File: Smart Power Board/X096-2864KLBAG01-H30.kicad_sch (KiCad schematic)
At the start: 12 parts, among them Q1 FDN338P, Q4 FDN335N

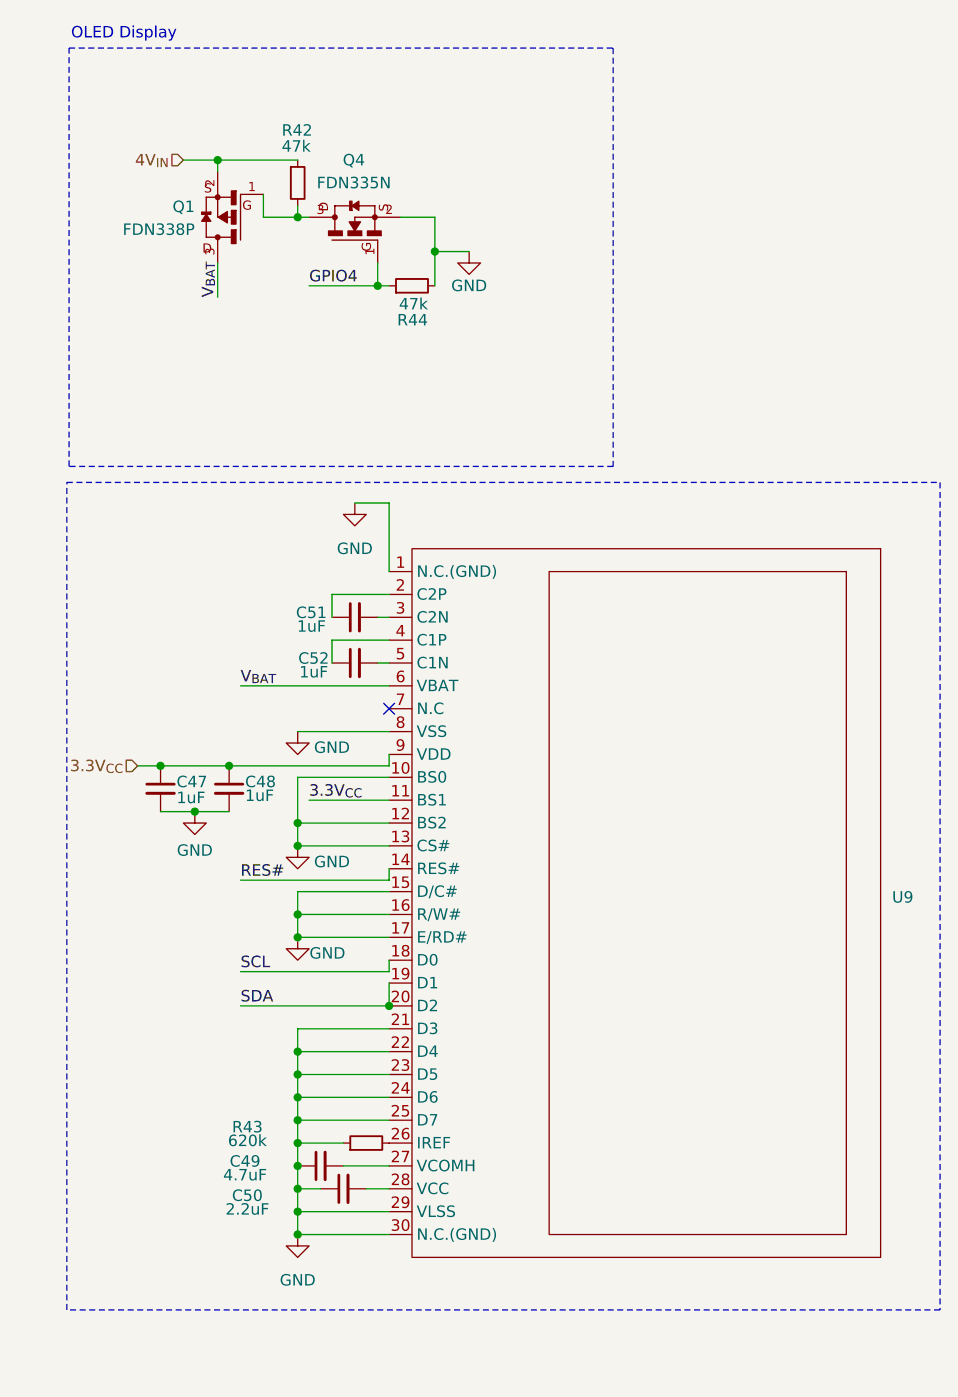
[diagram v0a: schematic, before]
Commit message: Feat[SmartPowerBoard]: Routing
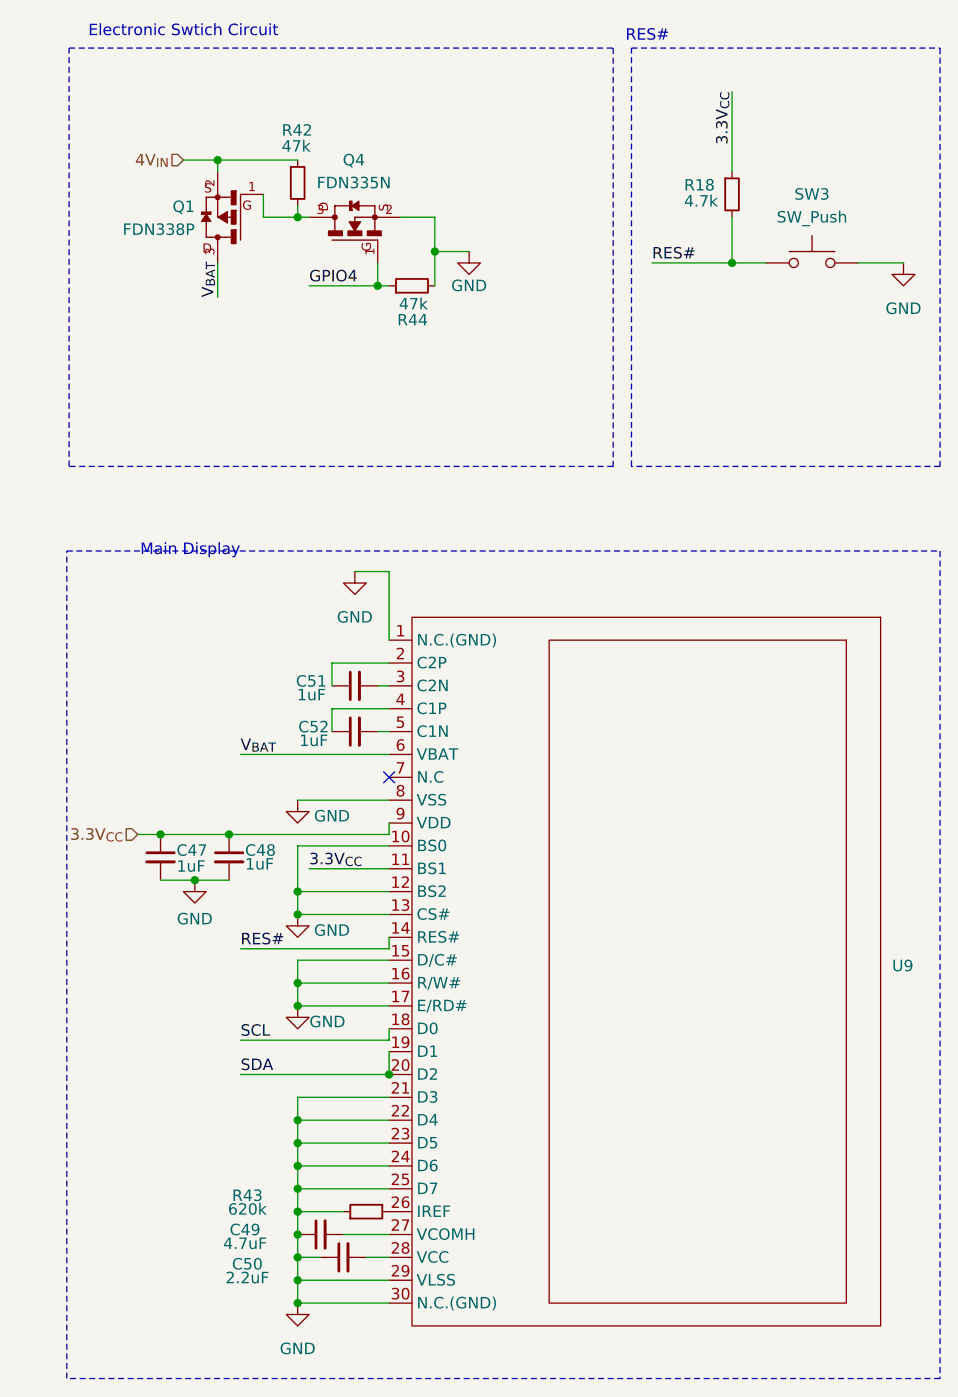
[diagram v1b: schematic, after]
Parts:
- added R18: 4.7k, Resistor_SMD:R_0402_1005Metric, symbol Device:R_Small
- added SW3: SW_Push, Button_Switch_SMD:SW_Push_SPST_NO_Alps_SKRK, symbol Switch:SW_Push
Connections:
- net 3.3V_{CC}: now also R18.1
- net GND: now also SW3.2
- net RES#: now also R18.2, SW3.1
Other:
- note added: "Electronic Swtich Circuit"
- note added: "Main Display"
- note added: "RES#"
- note removed: "OLED Display"
- moved on the sheet: C47, C48, C49, C50, C51, C52, R43, U9

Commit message: Feat[SmartPowerBoard]: Routing Complete
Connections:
- net GPIO4 renamed GPIO15
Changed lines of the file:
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@@
 	(wire
 		(pts
-			(xy 86.36 62.23) (xy 93.98 62.23)
+			(xy 91.44 62.23) (xy 93.98 62.23)
 		)
 		(stroke
@@
 		)
 	)
-	(label "SCL"
-		(at 78.74 146.05 0)
-		(fields_autoplaced yes)
-		(effects
-			(font
-				(size 1.27 1.27)
-			)
-			(justify left bottom)
-		)
-	)
 	(label "RES#"
 		(at 124.46 59.69 0)
@@
 		)
 	)
-	(label "SDA"
-		(at 78.74 149.86 0)
-		(fields_autoplaced yes)
-		(effects
-			(font
-				(size 1.27 1.27)
-			)
-			(justify left bottom)
-		)
-	)
 	(label "V_{BAT}"
 		(at 76.2 63.5 90)
@@
 		)
 	)
-	(label "GPIO4"
-		(at 86.36 62.23 0)
-		(fields_autoplaced yes)
-		(effects
-			(font
-				(size 1.27 1.27)
-			)
-			(justify left bottom)
-		)
-	)
 	(label "RES#"
 		(at 78.74 135.89 0)
@@
 			)
 			(justify right bottom)
+		)
+	)
+	(hierarchical_label "SDA"
+		(shape bidirectional)
+		(at 78.74 149.86 180)
+		(fields_autoplaced yes)
+		(effects
+			(font
+				(size 1.27 1.27)
+			)
+			(justify right)
 		)
 	)
@@
 		(fields_autoplaced yes)
 		(effects
+			(font
+				(size 1.27 1.27)
+			)
+			(justify right)
+		)
+	)
+	(hierarchical_label "SCL"
+		(shape bidirectional)
+		(at 78.74 146.05 180)
+		(fields_autoplaced yes)
+		(effects
+			(font
+				(size 1.27 1.27)
+			)
+			(justify right)
+		)
+	)
+	(hierarchical_label "GPIO15"
+		(shape input)
+		(at 91.44 62.23 180)
+		(fields_autoplaced yes)
+		(effects
